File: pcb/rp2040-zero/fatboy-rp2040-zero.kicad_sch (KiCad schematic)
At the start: 76 parts, among them SW1 SW_Push, U1 Helios

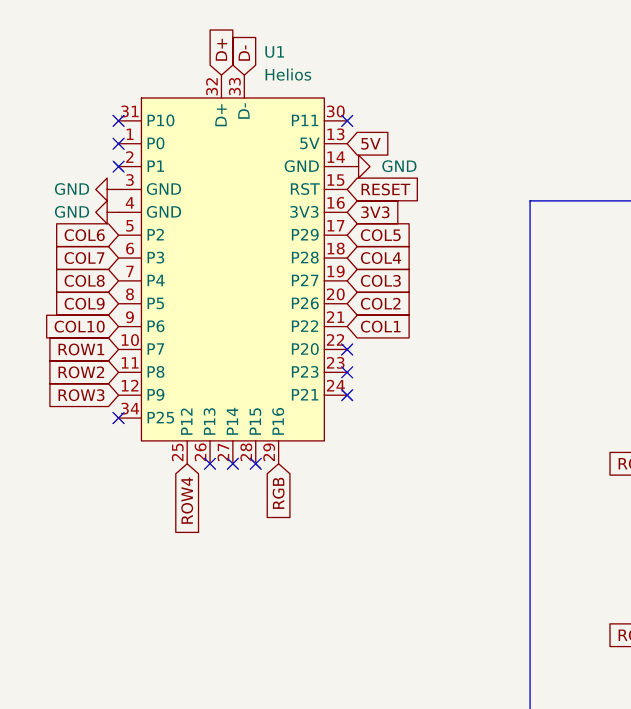
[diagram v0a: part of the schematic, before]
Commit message: sch: update symbol from helios to rp2040-zero
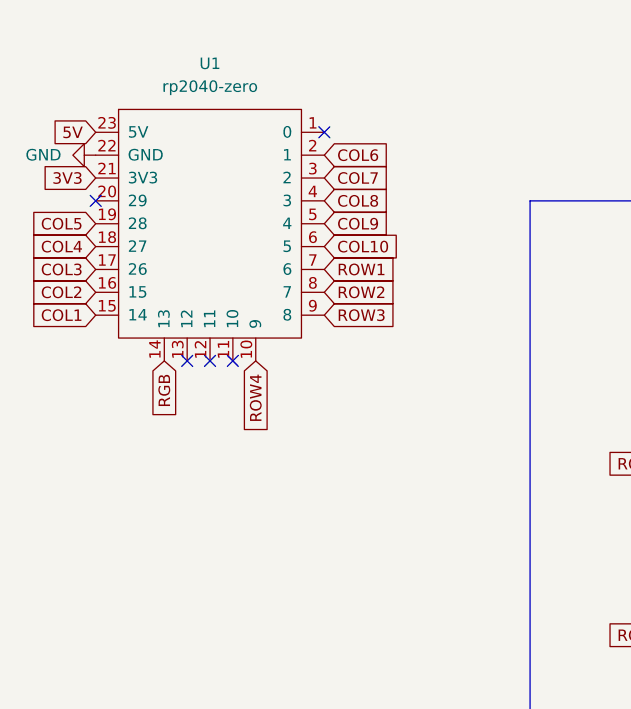
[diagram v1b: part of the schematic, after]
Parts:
- removed U1: Helios, PCM_marbastlib-xp-promicroish:Helios_AH_USBup, symbol marbastlib-promicroish:Helios
- added U1: rp2040-zero, mcu:rp2040-zero-tht, symbol kleeb-mcu:rp2040-zero
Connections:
- net 3V3: now also U1.21 (3V3)
- net 5V: now also U1.23 (5V)
- net COL1: now also U1.15 (14)
- net COL10: now also U1.6 (5)
- net COL2: now also U1.16 (15)
- net COL3: now also U1.17 (26)
- net COL4: now also U1.18 (27)
- net COL5: now also U1.19 (28)
- net COL6: now also U1.2 (1)
- net COL7: now also U1.3 (2)
- net COL8: now also U1.4 (3)
- net COL9: now also U1.5 (4)
- net GND: now also U1.22 (GND)
- net RGB: now also U1.14 (13)
- net ROW1: now also U1.7 (6)
- net ROW2: now also U1.8 (7)
- net ROW3: now also U1.9 (8)
- net ROW4: now also U1.10 (9)
- no-connect marks 12 -> 6

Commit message: reposition rows
Signed-off-by: Anant Thazhemadam <anant.thazhemadam@gmail.com>
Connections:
- net COL10: now also U1.9 (8); no longer U1.6 (5)
- net COL6: now also U1.5 (4); no longer U1.2 (1)
- net COL7: now also U1.6 (5); no longer U1.3 (2)
- net COL8: now also U1.7 (6); no longer U1.4 (3)
- net COL9: now also U1.8 (7); no longer U1.5 (4)
- net ROW1: now also U1.13 (12); no longer U1.7 (6)
- net ROW2: now also U1.12 (11); no longer U1.8 (7)
- net ROW3: now also U1.11 (10); no longer U1.9 (8)

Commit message: sch: replace global symbols with power symbols for power pins
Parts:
- added J1: Conn_01x08_Socket, symbol Connector:Conn_01x08_Socket
- added U2: 74HC595, symbol 74xx:74HC595
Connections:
- net COL1: now also U1.16 (15); no longer U1.15 (14)
- net COL10: now also U1.5 (4); no longer U1.9 (8)
- net COL2: now also U1.17 (26); no longer U1.16 (15)
- net COL3: now also U1.18 (27); no longer U1.17 (26)
- net COL4: now also U1.19 (28); no longer U1.18 (27)
- net COL5: now also U1.20 (29); no longer U1.19 (28)
- net COL6: now also U1.1 (0); no longer U1.5 (4)
- net COL7: now also U1.2 (1); no longer U1.6 (5)
- net COL8: now also U1.3 (2); no longer U1.7 (6)
- net COL9: now also U1.4 (3); no longer U1.8 (7)
- net GND: now also U2.13 (~{OE}), U2.8 (GND)
- net 3V3 renamed +3V3
- net +3V3: now also U2.10 (~{SRCLR}), U2.16 (VCC)
- net 5V renamed +5V
- new net: J1.2 (Pin_2), U2.1 (QB)
- new net: J1.1 (Pin_1), U2.15 (QA)
- new net: J1.3 (Pin_3), U2.2 (QC)
- new net: J1.4 (Pin_4), U2.3 (QD)
- new net: J1.5 (Pin_5), U2.4 (QE)
- new net: J1.6 (Pin_6), U2.5 (QF)
- new net: J1.7 (Pin_7), U2.6 (QG)
- new net: J1.8 (Pin_8), U2.7 (QH)
- new net AUDIO: U1.15 (14)
- new net MOSI: U1.7 (6), U2.14 (SER)
- new net SCLK: U1.8 (7), U2.11 (SRCLK)
- new net SPI_CS: U1.9 (8), U2.12 (RCLK)
- no-connect marks 6 -> 3
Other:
- moved on the sheet: D1, D10, D11, D12, D13, D14, D15, D16, D17, D18, D19, D2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

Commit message: sch: add labels for shift register and MCU
Signed-off-by: Anant Thazhemadam <anant.thazhemadam@gmail.com>
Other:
- note added: "74HC595"
- note added: "RP2040-Zero"
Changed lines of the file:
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@@
+	)
+	(rectangle
+		(start 12.954 71.374)
+		(end 76.454 124.46)
+		(stroke
+			(width 0)
+			(type default)
+		)
+		(fill
+			(type none)
+		)
+	)
+	(rectangle
+		(start 12.7 22.86)
+		(end 61.468 68.834)
+		(stroke
+			(width 0)
+			(type default)
+		)
+		(fill
+			(type none)
+		)
 	)
 	(rectangle
@@
 		)
 	)
+	(text "RP2040-Zero"
+		(exclude_from_sim no)
+		(at 47.498 67.31 0)
+		(effects
+			(font
+				(size 1.27 1.27)
+			)
+			(justify left bottom)
+		)
+	)
+	(text "74HC595"
+		(exclude_from_sim no)
+		(at 66.548 123.19 0)
+		(effects
+			(font
+				(size 1.27 1.27)
+			)
+			(justify left bottom)
+		)
+	)

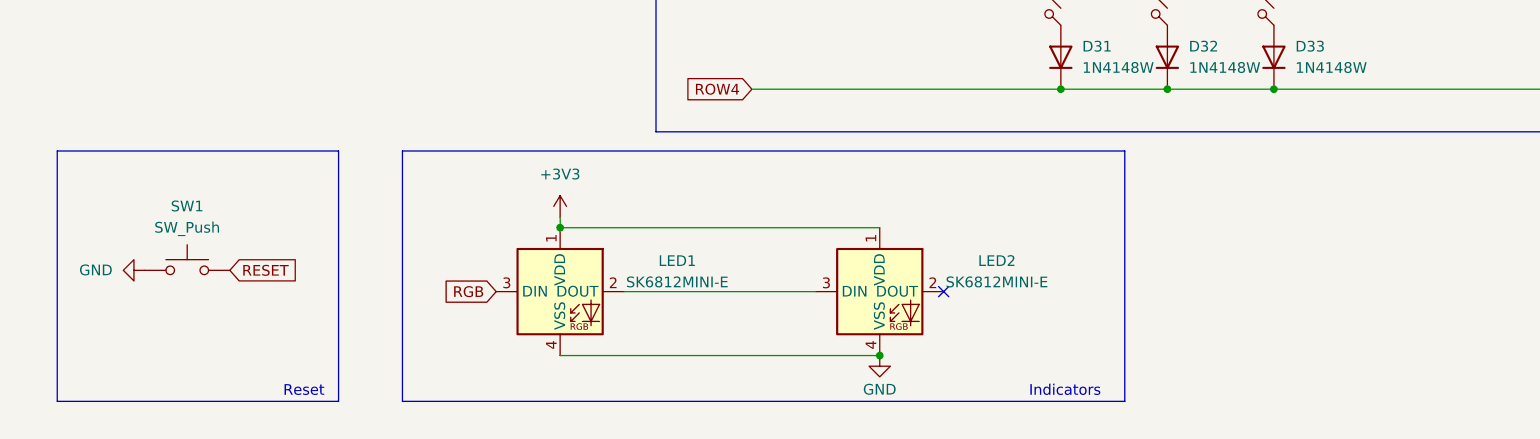
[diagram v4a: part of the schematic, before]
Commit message: sch: remove RESET switch and rearrange LED
Note: The RESET switch is removed since the RP2040-Zero doesn't have
a pin for it anyways.
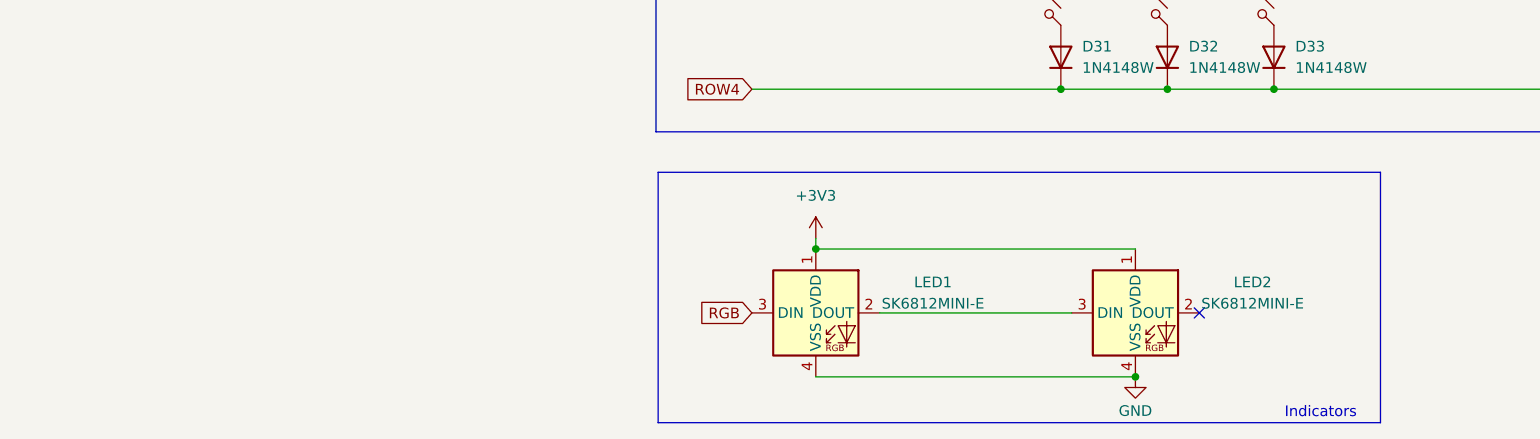
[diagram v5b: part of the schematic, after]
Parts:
- removed SW1: SW_Push, marbastlib-various:SW_SKHLLCA010, symbol Switch:SW_Push
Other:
- note removed: "Reset"
- moved on the sheet: LED1, LED2

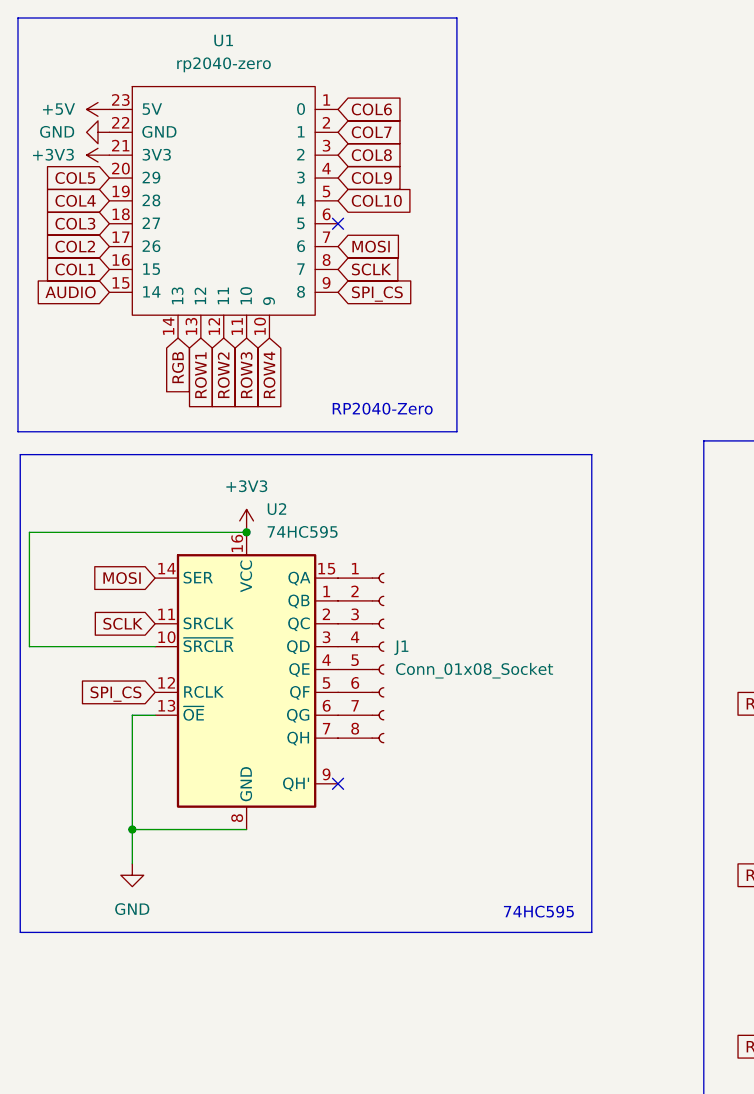
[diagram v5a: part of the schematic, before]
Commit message: rp2040-zero: finish up design
* Move rows and column labels to digital pins instead of analog, since
the latter has been reported to apparently have random issues with
registering keypresses sometimes
* Re-route tracks
* Remove unnecessary labels
* Remove shift register, since this will require a significant re-write
and re-routing for everything
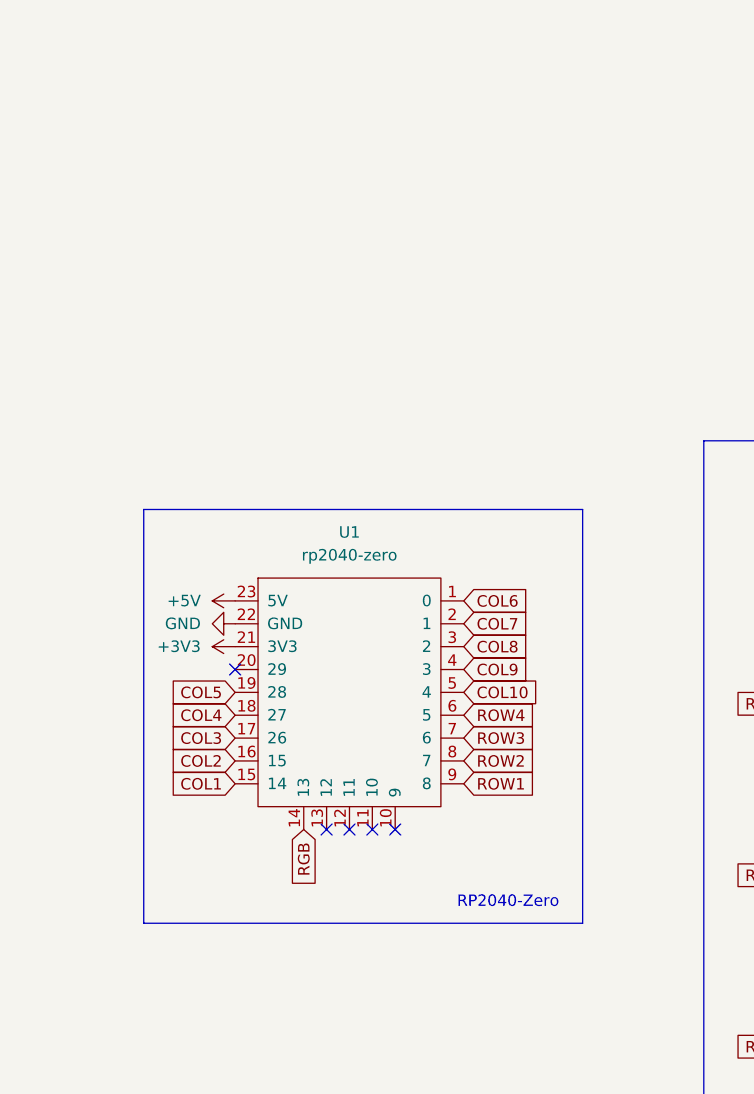
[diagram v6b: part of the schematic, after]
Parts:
- removed J1: Conn_01x08_Socket, symbol Connector:Conn_01x08_Socket
- removed U2: 74HC595, symbol 74xx:74HC595
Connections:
- net AUDIO is gone; now on net COL1: U1.15 (14)
- net MOSI is gone; now on net ROW3: U1.7 (6)
- net SCLK is gone; now on net ROW2: U1.8 (7)
- net SPI_CS is gone; now on net ROW1: U1.9 (8)
- net COL1: no longer U1.16 (15)
- net COL2: now also U1.16 (15); no longer U1.17 (26)
- net COL3: now also U1.17 (26); no longer U1.18 (27)
- net COL4: now also U1.18 (27); no longer U1.19 (28)
- net COL5: now also U1.19 (28); no longer U1.20 (29)
- net ROW1: no longer U1.13 (12)
- net ROW2: no longer U1.12 (11)
- net ROW3: no longer U1.11 (10)
- net ROW4: now also U1.6 (5); no longer U1.10 (9)
- no-connect marks 3 -> 6
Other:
- note removed: "74HC595"
- moved on the sheet: U1
